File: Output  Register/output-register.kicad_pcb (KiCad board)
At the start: 2 copper layers, 72.4 x 74.9 mm, 35 parts, among them J1 Bus, J2 Power, J3 Misc, SW1 Negative, U1 74LS08, U10 HDSP-7403, U2 LM555, U3 74LS273, U4 74LS76, U5 24C16, U6 74LS139, U7 HDSP-7403, U8 HDSP-7403, U9 HDSP-7403

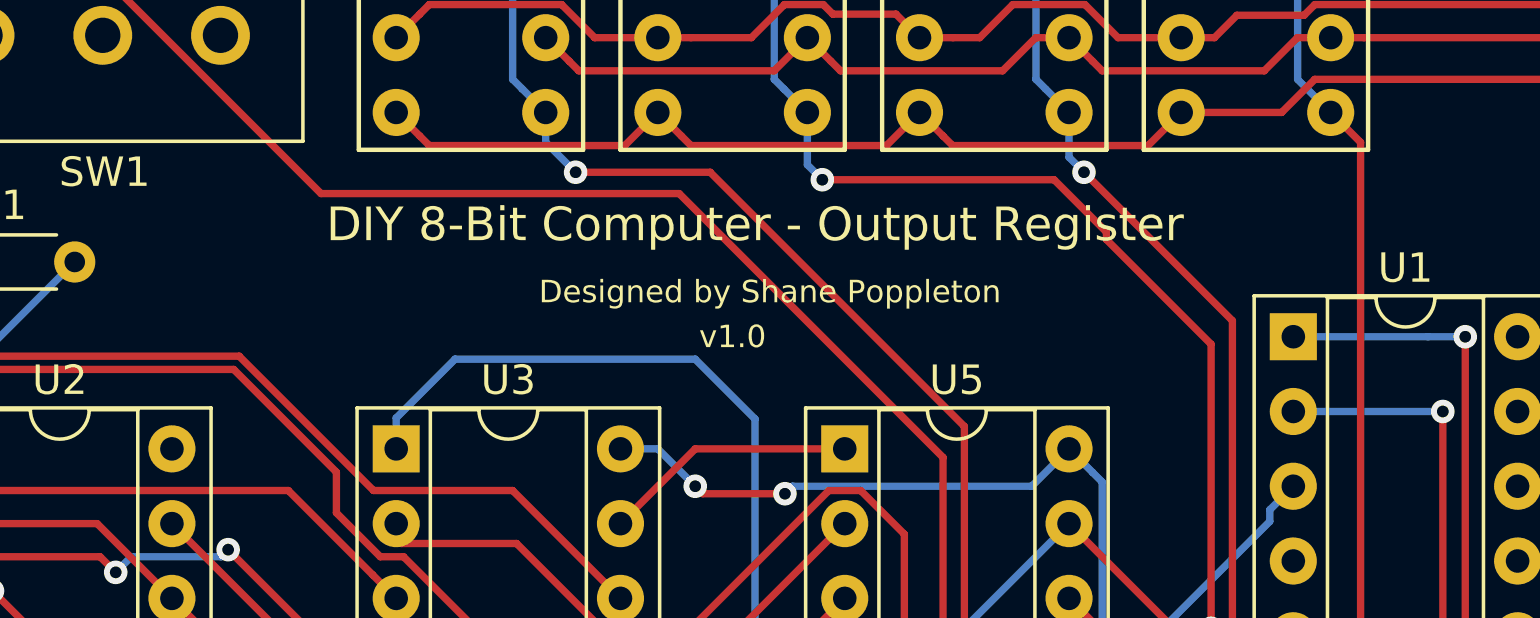
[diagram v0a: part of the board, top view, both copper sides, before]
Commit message: Added Attribution on each PCB, and regenerated gerbers
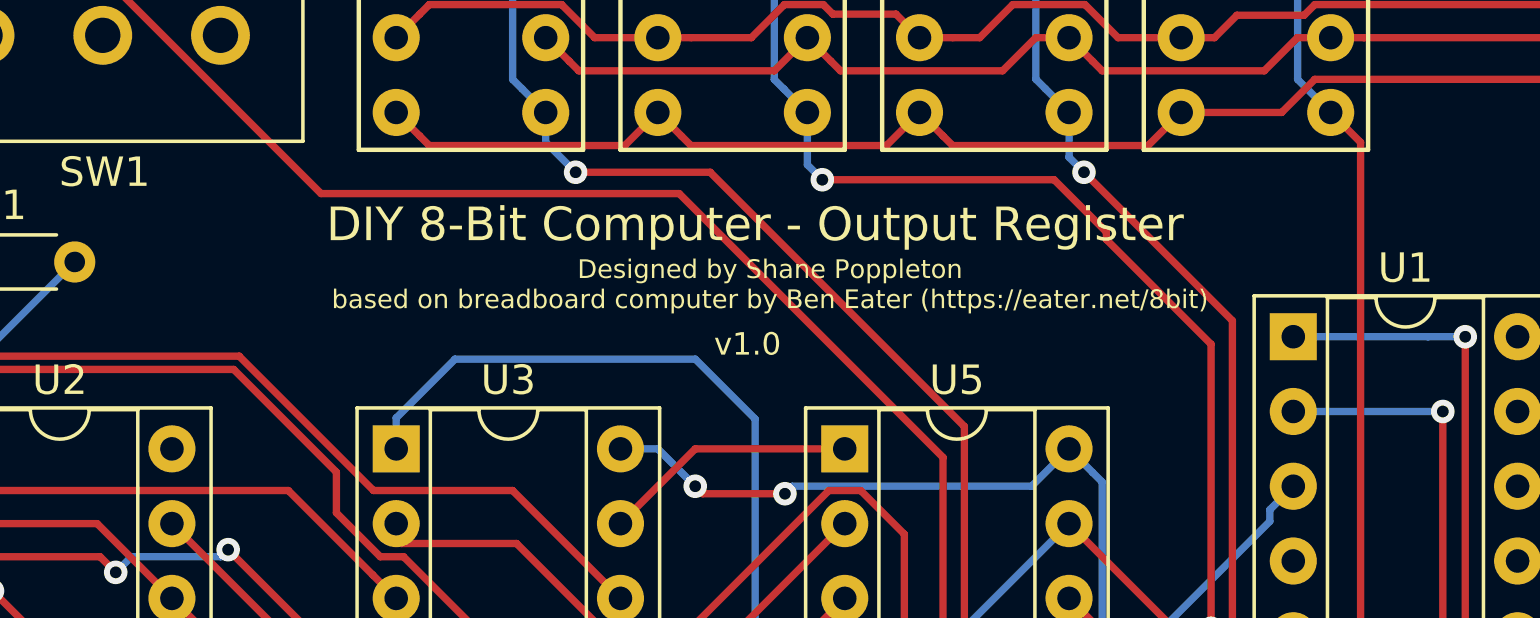
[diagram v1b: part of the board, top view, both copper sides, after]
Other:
- board text added: "Designed by Shane Poppleton based on breadboard computer by Ben Eater (https://eater.net/8bit)"
- board text removed: "Designed by Shane Poppleton"
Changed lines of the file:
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@@
     (effects (font (size 1 1) (thickness 0.15)))
   )
-  (gr_text v1.0 (at 148.082 84.328) (layer F.SilkS)
+  (gr_text v1.0 (at 148.59 84.582) (layer F.SilkS)
     (effects (font (size 0.762 0.762) (thickness 0.127)))
   )
-  (gr_text "Designed by Shane Poppleton" (at 149.352 82.804) (layer F.SilkS)
-    (effects (font (size 0.762 0.762) (thickness 0.127)))
+  (gr_text "Designed by Shane Poppleton\nbased on breadboard computer by Ben Eater (https://eater.net/8bit)\n" (at 149.352 82.55) (layer F.SilkS)
+    (effects (font (size 0.635 0.635) (thickness 0.1016)))
   )
   (gr_text "DIY 8-Bit Computer - Output Register" (at 148.844 80.518) (layer F.SilkS)
